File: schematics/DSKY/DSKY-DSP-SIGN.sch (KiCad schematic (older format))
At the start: 16 parts, among them U17 74LS02, U38 74LS74, U39 74LS74, U41 74LS74, U44 74LS08, U45 74LS04, U46 74LS04, U50 74LS244, U60 74LS126, U64 74LS00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

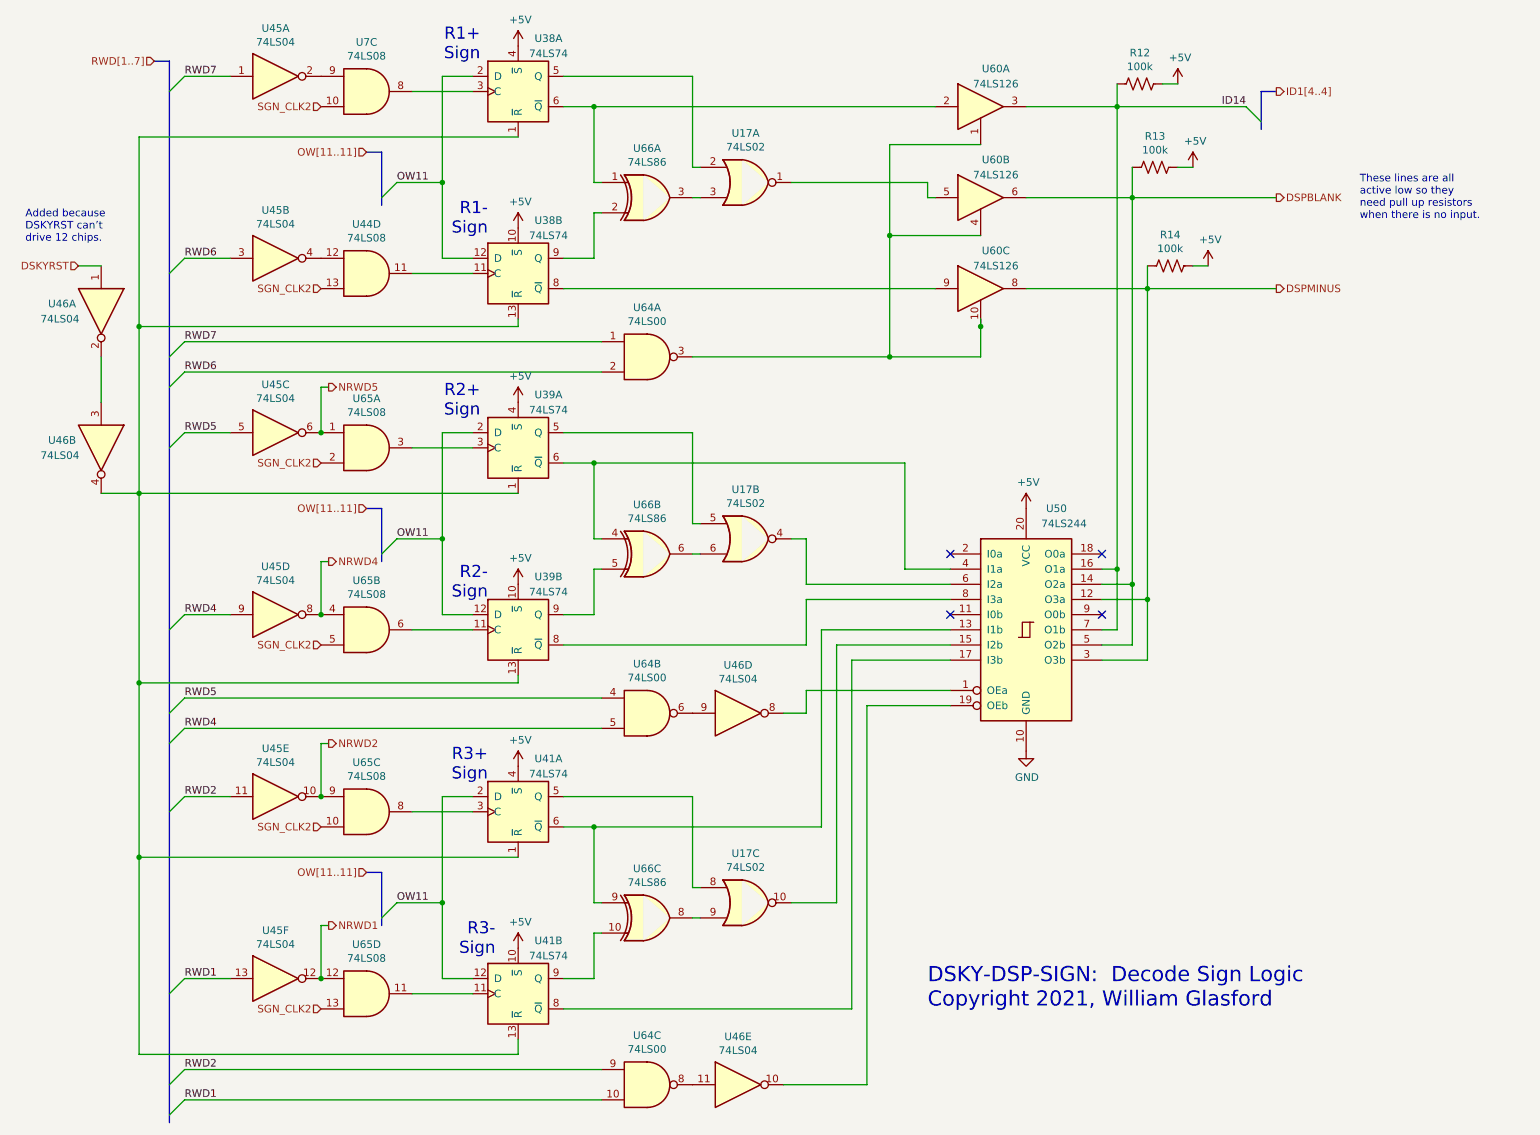
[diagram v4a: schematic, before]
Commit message: Using 4 LED driver chips.
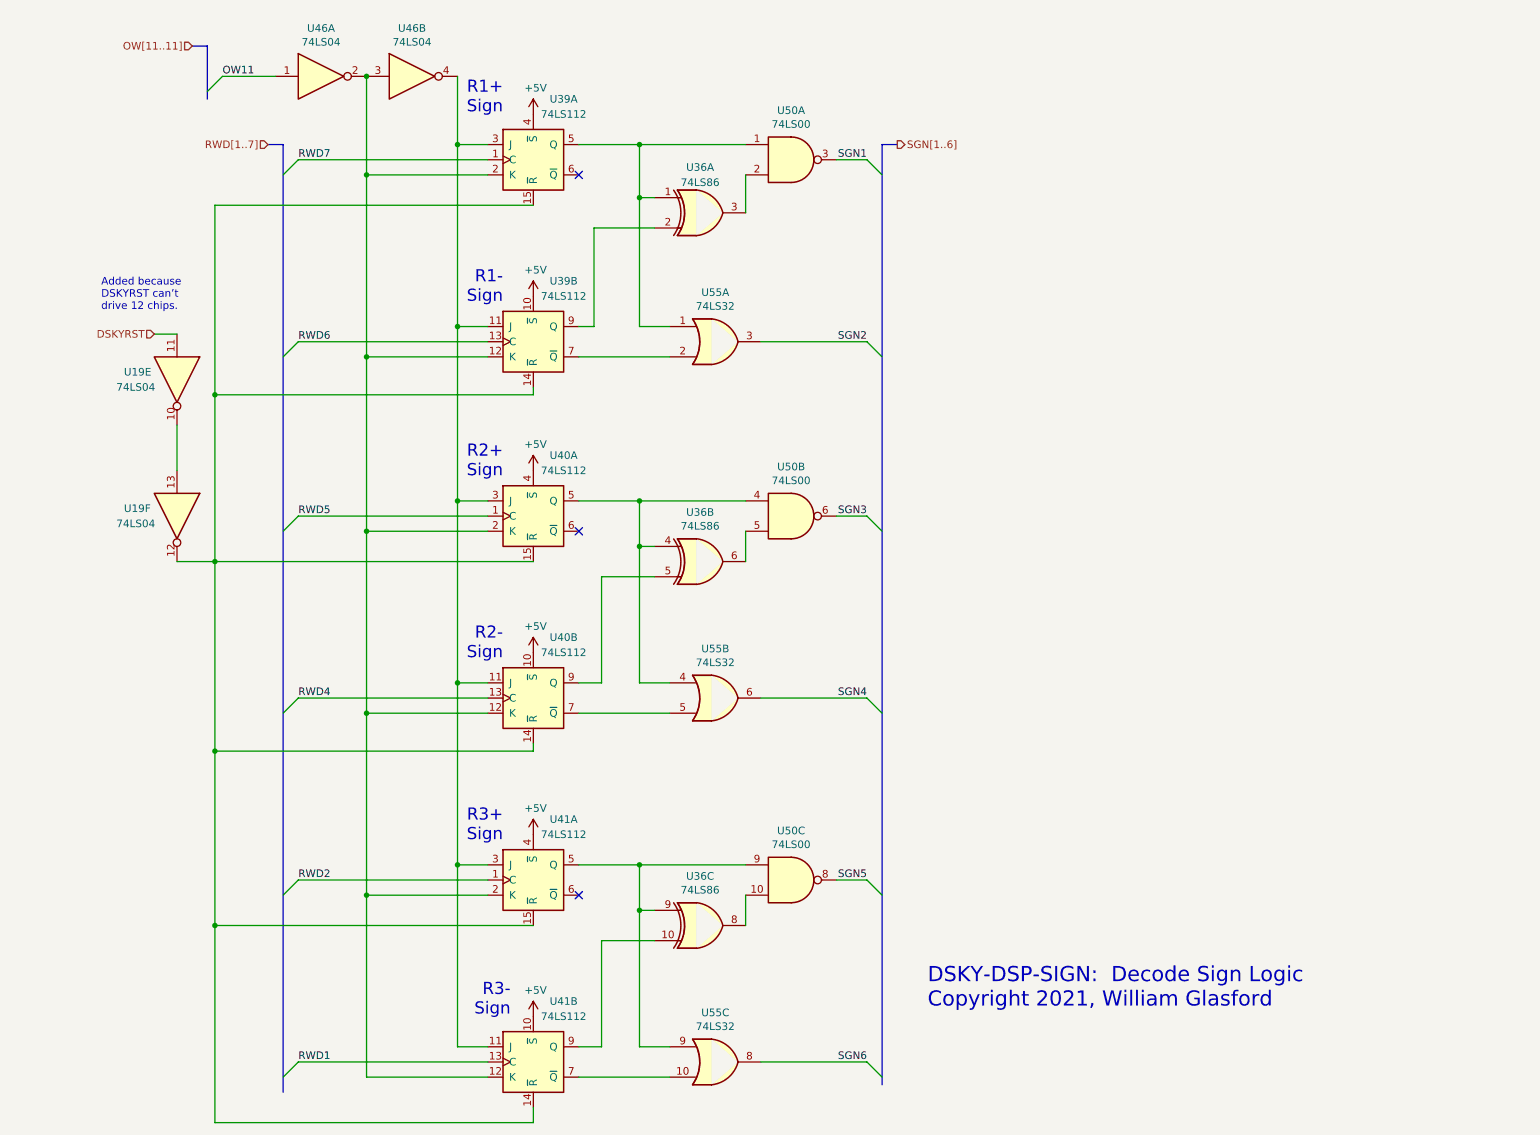
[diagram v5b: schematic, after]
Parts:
- removed R12, R13, R14: 100k, symbol Device:R_US
- removed U17: 74LS02, symbol 74xx:74LS02
- removed U38, U39, U41: 74LS74, symbol 74xx:74LS74
- removed U44, U65, U7: 74LS08, symbol 74xx:74LS08
- removed U45: 74LS04, symbol 74xx:74LS04
- removed unit 4 of U46
- removed unit 5 of U46
- removed U50: 74LS244, symbol 74xx:74LS244
- removed U60: 74LS126, symbol 74xx:74LS126
- removed U64: 74LS00, symbol 74xx:74LS00
- removed U66: 74LS86, symbol 74xx:74LS86
- added U36: 74LS86, symbol 74xx:74LS86
- added U39, U40, U41: 74LS112, symbol 74xx:74LS112
- added U46: 74LS04, symbol 74xx:74LS04
- added U50: 74LS00, symbol 74xx:74LS00
- added U55: 74LS32, symbol 74xx:74LS32
- renumbered U46 to U19
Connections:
- net +5V: now also U39.10 (~S), U39.4 (~S), U40.10 (~S), U40.4 (~S), U41.10 (~S), U41.4 (~S)
- net DSKYRST: now also U19.11; no longer U19.1
- net OW11: now also U46.1
- net RWD1: now also U41.13 (C)
- net RWD2: now also U41.1 (C)
- net RWD4: now also U40.13 (C)
- net RWD5: now also U40.1 (C)
- net RWD6: now also U39.13 (C)
- net RWD7: now also U39.1 (C)
- new net: U19.10, U19.13
- new net: U19.12, U39.14 (~R), U39.15 (~R), U40.14 (~R), U40.15 (~R), U41.14 (~R), U41.15 (~R)
- new net: U39.12 (K), U39.2 (K), U40.12 (K), U40.2 (K), U41.12 (K), U41.2 (K), U46.2, U46.3
- new net: U39.11 (J), U39.3 (J), U40.11 (J), U40.3 (J), U41.11 (J), U41.3 (J), U46.4
- new net: U36.1, U39.5 (Q), U50.1, U55.1
- new net: U39.7 (~Q), U55.2
- new net: U36.2, U39.9 (Q)
- new net: U36.4, U40.5 (Q), U50.4, U55.4
- new net: U36.9, U41.5 (Q), U50.9, U55.9
- new net: U40.7 (~Q), U55.5
- new net: U36.5, U40.9 (Q)
- new net: U41.7 (~Q), U55.10
- new net: U36.10, U41.9 (Q)
- new net: U36.3, U50.2
- new net: U36.6, U50.5
- new net: U36.8, U50.10
- new net SGN1: U50.3
- new net SGN2: U55.3
- new net SGN3: U50.6
- new net SGN4: U55.6
- new net SGN5: U50.8
- new net SGN6: U55.8
- no-connect marks 4 -> 3
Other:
- note removed: "These lines are all \nactive low so they \nneed pull up resistors \nwhen there is no input."

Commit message: Modified to use fourth display decoder chip.
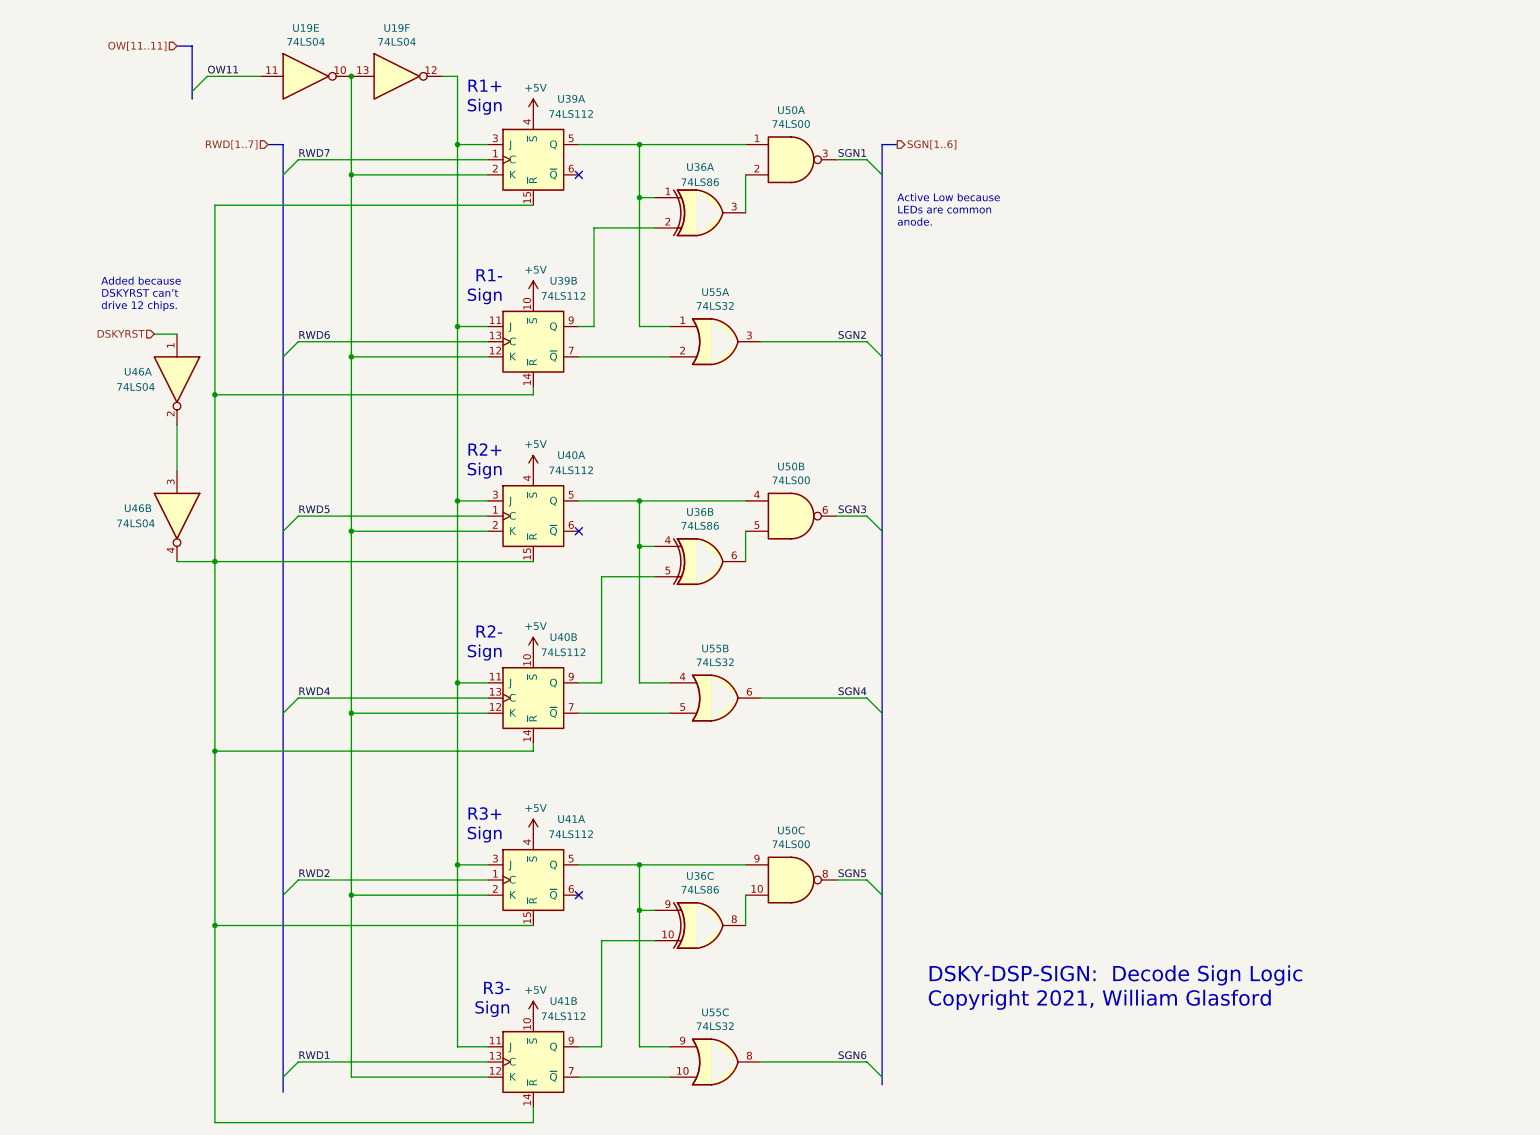
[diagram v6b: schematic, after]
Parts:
- removed U46: 74LS04, symbol 74xx:74LS04
- added U19: 74LS04, symbol 74xx:74LS04
- renumbered U19 to U46
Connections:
- net DSKYRST: now also U46.1; no longer U46.11
- net OW11: now also U19.11
- net at U39.14 (~R), U39.15 (~R), U40.14 (~R)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: now also U46.4; no longer U46.12
- net at U39.12 (K), U39.2 (K), U40.12 (K)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: now also U19.10, U19.13
- net at U39.11 (J), U39.3 (J), U40.11 (J)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: now also U19.12
- new net: U46.2, U46.3
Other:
- note added: "Active Low because\nLEDs are common\nanode."
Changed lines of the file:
@@
 $Descr A 11000 8500
 encoding utf-8
-Sheet 6 13
+Sheet 6 14
 Title ""
 Date ""
@@
 	3400 2650 3600 2650
 Wire Bus Line
-	1750 800  1650 800
-Entry Wire Line
-	1750 1100 1850 1000
-Text HLabel 1650 800  0    50   Input ~ 0
+	1650 800  1550 800
+Entry Wire Line
+	1650 1100 1750 1000
+Text HLabel 1550 800  0    50   Input ~ 0
 OW[11..11]
-Text Label 1850 1000 0    50   ~ 0
+Text Label 1750 1000 0    50   ~ 0
 OW11
 Text HLabel 1400 2700 0    50   Input ~ 0
@@
 RWD1
 $Comp
-L 74xx:74LS04 U19
-U 5 1 61E3EBB4
+L 74xx:74LS04 U46
+U 1 1 61E3EBB4
 P 1550 3000
-F 0 "U19" V 1500 2650 50  0000 L CNN
+F 0 "U46" V 1500 2650 50  0000 L CNN
 F 1 "74LS04" V 1600 2600 50  0000 L CNN
 F 2 "" H 1550 3000 50  0001 C CNN
 F 3 "http://www.ti.com/lit/gpn/sn74LS04" H 1550 3000 50  0001 C CNN
-	5    1550 3000
+	1    1550 3000
 	0    1    1    0
 $EndComp
@@
 	1800 6600 3900 6600
 $Comp
-L 74xx:74LS04 U19
-U 6 1 61F37E2B
+L 74xx:74LS04 U46
+U 2 1 61F37E2B
 P 1550 3900
-F 0 "U19" V 1500 3550 50  0000 L CNN
+F 0 "U46" V 1500 3550 50  0000 L CNN
 F 1 "74LS04" V 1600 3500 50  0000 L CNN
 F 2 "" H 1550 3900 50  0001 C CNN
 F 3 "http://www.ti.com/lit/gpn/sn74LS04" H 1550 3900 50  0001 C CNN
-	6    1550 3900
+	2    1550 3900
 	0    1    1    0
 $EndComp
@@
 	3400 1450 3400 1000
 Wire Wire Line
-	1850 1000 2200 1000
+	1750 1000 2100 1000
 Connection ~ 3400 1450
 $Comp
@@
 Text Label 6100 6300 2    50   ~ 0
 SGN5
-$Comp
-L 74xx:74LS112 U39
-U 1 1 626BEF81
-P 3900 1550
-F 0 "U39" H 4100 1950 50  0000 C CNN
-F 1 "74LS112" H 4100 1850 50  0000 C CNN
-F 2 "" H 3900 1550 50  0001 C CNN
-F 3 "http://www.ti.com/lit/gpn/sn74LS112" H 3900 1550 50  0001 C CNN
-	1    3900 1550
-	1    0    0    -1
-$EndComp
-$Comp
-L 74xx:74LS112 U39
-U 2 1 626C25BB
-P 3900 2750
-F 0 "U39" H 4100 3150 50  0000 C CNN
-F 1 "74LS112" H 4100 3050 50  0000 C CNN
-F 2 "" H 3900 2750 50  0001 C CNN
-F 3 "http://www.ti.com/lit/gpn/sn74LS112" H 3900 2750 50  0001 C CNN
-	2    3900 2750
-	1    0    0    -1
-$EndComp
-$Comp
-L 74xx:74LS112 U40
-U 1 1 626C5D5F
-P 3900 3900
-F 0 "U40" H 4100 4300 50  0000 C CNN
-F 1 "74LS112" H 4100 4200 50  0000 C CNN
-F 2 "" H 3900 3900 50  0001 C CNN
-F 3 "http://www.ti.com/lit/gpn/sn74LS112" H 3900 3900 50  0001 C CNN
-	1    3900 3900
-	1    0    0    -1
-$EndComp
-$Comp
-L 74xx:74LS112 U41
-U 1 1 626C6F74
-P 3900 6300
-F 0 "U41" H 4100 6700 50  0000 C CNN
-F 1 "74LS112" H 4100 6600 50  0000 C CNN
-F 2 "" H 3900 6300 50  0001 C CNN
-F 3 "http://www.ti.com/lit/gpn/sn74LS112" H 3900 6300 50  0001 C CNN
-	1    3900 6300
-	1    0    0    -1
-$EndComp
-$Comp
-L 74xx:74LS112 U40
-U 2 1 626C82D7
-P 3900 5100
-F 0 "U40" H 4100 5500 50  0000 C CNN
-F 1 "74LS112" H 4100 5400 50  0000 C CNN
-F 2 "" H 3900 5100 50  0001 C CNN
-F 3 "http://www.ti.com/lit/gpn/sn74LS112" H 3900 5100 50  0001 C CNN
-	2    3900 5100
-	1    0    0    -1
-$EndComp
-$Comp
-L 74xx:74LS112 U41
-U 2 1 626C9029
-P 3900 7500
-F 0 "U41" H 4100 7900 50  0000 C CNN
-F 1 "74LS112" H 4100 7800 50  0000 C CNN
-F 2 "" H 3900 7500 50  0001 C CNN
-F 3 "http://www.ti.com/lit/gpn/sn74LS112" H 3900 7500 50  0001 C CNN
-	2    3900 7500
-	1    0    0    -1
-$EndComp
-$Comp
-L 74xx:74LS04 U46
-U 1 1 626CC42D
-P 2500 1000
-F 0 "U46" H 2500 1317 50  0000 C CNN
-F 1 "74LS04" H 2500 1226 50  0000 C CNN
-F 2 "" H 2500 1000 50  0001 C CNN
-F 3 "http://www.ti.com/lit/gpn/sn74LS04" H 2500 1000 50  0001 C CNN
-	1    2500 1000
-	1    0    0    -1
-$EndComp
-$Comp
-L 74xx:74LS04 U46
-U 2 1 626CCA7F
-P 3100 1000
-F 0 "U46" H 3100 1317 50  0000 C CNN
-F 1 "74LS04" H 3100 1226 50  0000 C CNN
-F 2 "" H 3100 1000 50  0001 C CNN
-F 3 "http://www.ti.com/lit/gpn/sn74LS04" H 3100 1000 50  0001 C CNN
-	2    3100 1000
-	1    0    0    -1
-$EndComp
-Wire Wire Line
-	3600 1650 2800 1650
-Wire Wire Line
-	2800 1650 2800 1000
-Connection ~ 2800 1000
-Wire Wire Line
-	2800 1650 2800 2850
-Wire Wire Line
-	2800 2850 3600 2850
-Connection ~ 2800 1650
-Wire Wire Line
-	2800 2850 2800 4000
-Wire Wire Line
-	2800 4000 3600 4000
-Connection ~ 2800 2850
-Wire Wire Line
-	2800 4000 2800 5200
-Wire Wire Line
-	2800 5200 3600 5200
-Connection ~ 2800 4000
-Wire Wire Line
-	2800 5200 2800 6400
-Wire Wire Line
-	2800 6400 3600 6400
-Connection ~ 2800 5200
-Wire Wire Line
-	2800 6400 2800 7600
-Wire Wire Line
-	2800 7600 3600 7600
-Connection ~ 2800 6400
 Wire Wire Line
 	2350 1550 3600 1550
@@
 	5300 6400 5300 6600
 NoConn ~ 4200 6400
+Text Notes 6300 2000 0    50   ~ 0
+Active Low because\nLEDs are common\nanode.
+$Comp
+L 74xx:74LS112 U39
+U 1 1 6291C61B
+P 3900 1550
+F 0 "U39" H 4150 1950 50  0000 C CNN
+F 1 "74LS112" H 4150 1850 50  0000 C CNN
+F 2 "" H 3900 1550 50  0001 C CNN
+F 3 "http://www.ti.com/lit/gpn/sn74LS112" H 3900 1550 50  0001 C CNN
+	1    3900 1550
+	1    0    0    -1
+$EndComp
+$Comp
+L 74xx:74LS112 U39
+U 2 1 6291D5F9
+P 3900 2750
+F 0 "U39" H 4100 3150 50  0000 C CNN
+F 1 "74LS112" H 4100 3050 50  0000 C CNN
+F 2 "" H 3900 2750 50  0001 C CNN
+F 3 "http://www.ti.com/lit/gpn/sn74LS112" H 3900 2750 50  0001 C CNN
+	2    3900 2750
+	1    0    0    -1
+$EndComp
+$Comp
+L 74xx:74LS04 U19
+U 5 1 62923706
+P 2400 1000
+F 0 "U19" H 2400 1317 50  0000 C CNN
+F 1 "74LS04" H 2400 1226 50  0000 C CNN
+F 2 "" H 2400 1000 50  0001 C CNN
+F 3 "http://www.ti.com/lit/gpn/sn74LS04" H 2400 1000 50  0001 C CNN
+	5    2400 1000
+	1    0    0    -1
+$EndComp
+$Comp
+L 74xx:74LS04 U19
+U 6 1 629241D0
+P 3000 1000
+F 0 "U19" H 3000 1317 50  0000 C CNN
+F 1 "74LS04" H 3000 1226 50  0000 C CNN
+F 2 "" H 3000 1000 50  0001 C CNN
+F 3 "http://www.ti.com/lit/gpn/sn74LS04" H 3000 1000 50  0001 C CNN
+	6    3000 1000
+	1    0    0    -1
+$EndComp
+Wire Wire Line
+	3300 1000 3400 1000
+Wire Wire Line
+	3600 1650 2700 1650
+Wire Wire Line
+	2700 1650 2700 1000
+Connection ~ 2700 1000
+Wire Wire Line
+	3600 2850 2700 2850
+Wire Wire Line
+	2700 2850 2700 1650
+Connection ~ 2700 1650
+$Comp
+L 74xx:74LS112 U40
+U 1 1 6293B4B1
+P 3900 3900
+F 0 "U40" H 4150 4300 50  0000 C CNN
+F 1 "74LS112" H 4150 4200 50  0000 C CNN
+F 2 "" H 3900 3900 50  0001 C CNN
+F 3 "http://www.ti.com/lit/gpn/sn74LS112" H 3900 3900 50  0001 C CNN
+	1    3900 3900
+	1    0    0    -1
+$EndComp
+$Comp
+L 74xx:74LS112 U40
+U 2 1 6293BBF6
+P 3900 5100
+F 0 "U40" H 4100 5500 50  0000 C CNN
+F 1 "74LS112" H 4100 5400 50  0000 C CNN
+F 2 "" H 3900 5100 50  0001 C CNN
+F 3 "http://www.ti.com/lit/gpn/sn74LS112" H 3900 5100 50  0001 C CNN
+	2    3900 5100
+	1    0    0    -1
+$EndComp
+$Comp
+L 74xx:74LS112 U41
+U 1 1 6293C8D2
+P 3900 6300
+F 0 "U41" H 4150 6700 50  0000 C CNN
+F 1 "74LS112" H 4150 6600 50  0000 C CNN
+F 2 "" H 3900 6300 50  0001 C CNN
+F 3 "http://www.ti.com/lit/gpn/sn74LS112" H 3900 6300 50  0001 C CNN
+	1    3900 6300
+	1    0    0    -1
+$EndComp
+$Comp
+L 74xx:74LS112 U41
+U 2 1 6293EFDA
+P 3900 7500
+F 0 "U41" H 4100 7900 50  0000 C CNN
+F 1 "74LS112" H 4100 7800 50  0000 C CNN
+F 2 "" H 3900 7500 50  0001 C CNN
+F 3 "http://www.ti.com/lit/gpn/sn74LS112" H 3900 7500 50  0001 C CNN
+	2    3900 7500
+	1    0    0    -1
+$EndComp
+Wire Wire Line
+	3600 4000 2700 4000
+Wire Wire Line
+	2700 4000 2700 2850
+Connection ~ 2700 2850
+Wire Wire Line
+	3600 5200 2700 5200
+Wire Wire Line
+	2700 5200 2700 4000
+Connection ~ 2700 4000
+Wire Wire Line
+	3600 6400 2700 6400
+Wire Wire Line
+	2700 6400 2700 5200
+Connection ~ 2700 5200
+Wire Wire Line
+	3600 7600 2700 7600
+Wire Wire Line
+	2700 7600 2700 6400
+Connection ~ 2700 6400
 Wire Bus Line
-	1750 800  1750 1150
+	1650 800  1650 1150
 Wire Bus Line
 	2250 1450 2250 7700
